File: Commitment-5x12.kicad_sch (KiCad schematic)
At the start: 96 parts, among them J1 Conn_01x13, J2 Conn_01x13, J3 Conn_01x03, J4 Conn_01x04, J5 Conn_01x04, SW1 OS102011MS2QN1, SW2 RotaryEncoder

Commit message: updated footprints to include 3D cad files
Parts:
- J3: footprint lizard_libs:PinHeader_1x03_P2.54mm_Vertical -> lizard_libs:PinSocket_1x03_P2.54mm_Vertical
- MX1, MX10, MX11, MX12, MX13, MX14, MX15, MX16, MX17, MX18, MX19, MX2, MX20, MX21, MX22, MX23, MX24, MX25, MX26, MX27, MX28, MX29, MX3, MX31, MX32, MX33, MX34, MX36, MX37, MX38, MX39, MX4, MX40, MX41, MX42, MX43, MX44, MX45, MX46, MX47, MX48, MX49, MX5, MX50, MX51, MX52, MX53, MX54, MX55, MX56, MX57, MX58, MX59, MX6, MX60, MX7, MX8, MX9: footprint lizard_libs:hotswap_keyswitch_reflow -> lizard_libs:Kailh_MX_Hotswap_Socket

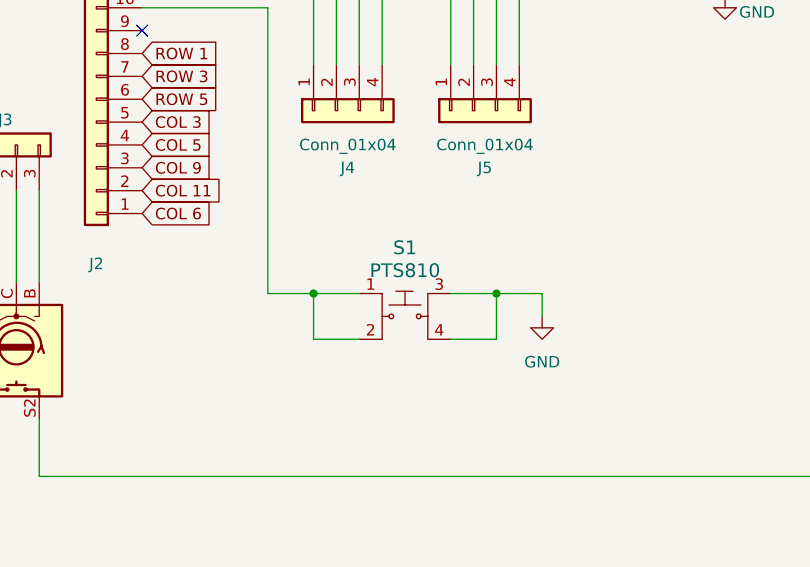
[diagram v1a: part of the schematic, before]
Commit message: Switched to B3F reset switch
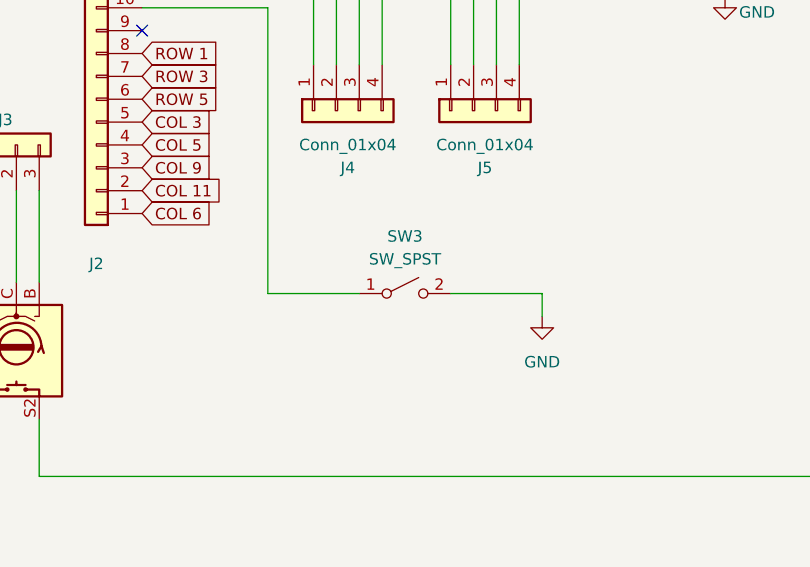
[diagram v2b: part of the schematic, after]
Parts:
- removed S1: PTS810, lizard_libs:PTS_180_Tactile_Switch, symbol lizard_lib:PTS810
- added SW3: SW_SPST, lizard_libs:Omron_B3F-1000, symbol Switch:SW_SPST
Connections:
- net GND: now also SW3.2 (B)
- net at J2.10 (Pin_10): now also SW3.1 (A)
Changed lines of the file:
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@@
 	)
 	(junction
-		(at 130.81 113.03)
-		(diameter 0)
-		(color 0 0 0 0)
-	)
-	(junction
 		(at 163.83 200.66)
 		(diameter 0)
@@
 	)
 	(junction
-		(at 110.49 113.03)
-		(diameter 0)
-		(color 0 0 0 0)
-	)
-	(junction
 		(at 176.53 194.31)
 		(diameter 0)
@@
 	(wire
 		(pts
-			(xy 130.81 118.11) (xy 130.81 113.03)
-		)
-		(stroke
-			(width 0)
-			(type default)
-		)
-	)
-	(wire
-		(pts
 			(xy 213.36 161.29) (xy 213.36 165.1)
 		)
@@
 	(wire
 		(pts
-			(xy 110.49 113.03) (xy 115.57 113.03)
-		)
-		(stroke
-			(width 0)
-			(type default)
-		)
-	)
-	(wire
-		(pts
 			(xy 156.21 80.01) (xy 156.21 78.74)
 		)
@@
 	(wire
 		(pts
-			(xy 110.49 118.11) (xy 115.57 118.11)
-		)
-		(stroke
-			(width 0)
-			(type default)
-		)
-	)
-	(wire
-		(pts
 			(xy 118.11 87.63) (xy 118.11 72.39)
 		)
@@
 	(wire
 		(pts
-			(xy 130.81 113.03) (xy 135.89 113.03)
+			(xy 125.73 113.03) (xy 135.89 113.03)
 		)
 		(stroke
@@
 	(wire
 		(pts
-			(xy 125.73 113.03) (xy 130.81 113.03)
-		)
-		(stroke
-			(width 0)
-			(type default)
-		)
-	)
-	(wire
-		(pts
 			(xy 160.02 212.09) (xy 176.53 212.09)
 		)
@@
 	(wire
 		(pts
-			(xy 105.41 113.03) (xy 110.49 113.03)
+			(xy 105.41 113.03) (xy 115.57 113.03)
 		)
 		(stroke
@@
 	(wire
 		(pts
-			(xy 125.73 118.11) (xy 130.81 118.11)
-		)
-		(stroke
-			(width 0)
-			(type default)
-		)
-	)
-	(wire
-		(pts
 			(xy 66.04 76.2) (xy 44.45 76.2)
 		)
@@
 	(wire
 		(pts
-			(xy 110.49 113.03) (xy 110.49 118.11)
-		)
-		(stroke
-			(width 0)
-			(type default)
-		)
-	)
-	(wire
-		(pts
 			(xy 127 194.31) (xy 143.51 194.31)
 		)
@@
 	)
 	(symbol
+		(lib_id "Switch:SW_SPST")
+		(at 120.65 113.03 0)
+		(unit 1)
+		(exclude_from_sim no)
+		(in_bom yes)
+		(on_board yes)
+		(dnp no)
+		(fields_autoplaced yes)
+		(property "Reference" "SW3"
+			(at 120.65 106.68 0)
+			(effects
+				(font
+					(size 1.27 1.27)
+				)
+			)
+		)
+		(property "Value" "SW_SPST"
+			(at 120.65 109.22 0)
+			(effects
+				(font
+					(size 1.27 1.27)
+				)
+			)
+		)
+		(property "Footprint" "lizard_libs:Omron_B3F-1000"
+			(at 120.65 113.03 0)
+			(effects
+				(font
+					(size 1.27 1.27)
+				)
+				(hide yes)
+			)
+		)
+		(property "Datasheet" "~"
+			(at 120.65 113.03 0)
+			(effects
+				(font
+					(size 1.27 1.27)
+				)
+				(hide yes)
+			)
+		)
+		(property "Description" "Single Pole Single Throw (SPST) switch"
+			(at 120.65 113.03 0)
+			(effects
+				(font
+					(size 1.27 1.27)
+				)
+				(hide yes)
+			)
+		)
+		(pin "1"
+		)
+		(pin "2"
+		)
+		(instances
+			(project ""
+				(path "/0dc486c7-2743-451e-93ad-8516174ce902"
+					(reference "SW3")
+					(unit 1)
+				)
+			)
+		)
+	)
+	(symbol
 		(lib_id "lizard_lib:MX_Switch")
 		(at 104.14 166.37 0)
@@
 					(unit 1)
 				)
-			)
-		)
-	)
-	(symbol
-		(lib_id "lizard_lib:PTS810")
-		(at 120.65 115.57 0)
-		(unit 1)
-		(exclude_from_sim no)
-		(in_bom yes)
-		(on_board yes)
-		(dnp no)
-		(fields_autoplaced yes)
-		(property "Reference" "S1"
-			(at 120.65 107.95 0)
-			(effects
-				(font
-					(size 1.524 1.524)
-				)
-			)
-		)
-		(property "Value" "PTS810"
-			(at 120.65 110.49 0)
-			(effects
-				(font
-					(size 1.524 1.524)
-				)
-			)
-		)
-		(property "Footprint" "lizard_libs:PTS_180_Tactile_Switch"
-			(at 125.73 110.49 0)
-			(effects
-				(font
-					(size 1.524 1.524)
-				)
-				(justify left)
-				(hide yes)
-			)
-		)
-		(property "Datasheet" ""
-			(at 125.73 107.95 0)
-			(effects
-				(font
-					(size 1.524 1.524)
-				)
-				(justify left)
-				(hide yes)
-			)
-		)
-		(property "Description" "SWITCH TACTILE SPST-NO 0.05A 24V"
-			(at 120.65 115.57 0)
-			(effects
-				(font
-					(size 1.27 1.27)
-				)
-				(hide yes)
-			)
-		)
-		(property "Location" "Denali-H2"
-			(at 120.65 115.57 0)
-			(effects
-				(font
-					(size 1.27 1.27)
-				)
-				(hide yes)
-			)
-		)
-		(pin "4"
-		)
-		(pin "1"
-		)
-		(pin "2"
-		)
-		(pin "3"
-		)
-		(instances
-			(project ""
-				(path "/0dc486c7-2743-451e-93ad-8516174ce902"
-					(reference "S1")
-					(unit 1)
-				)

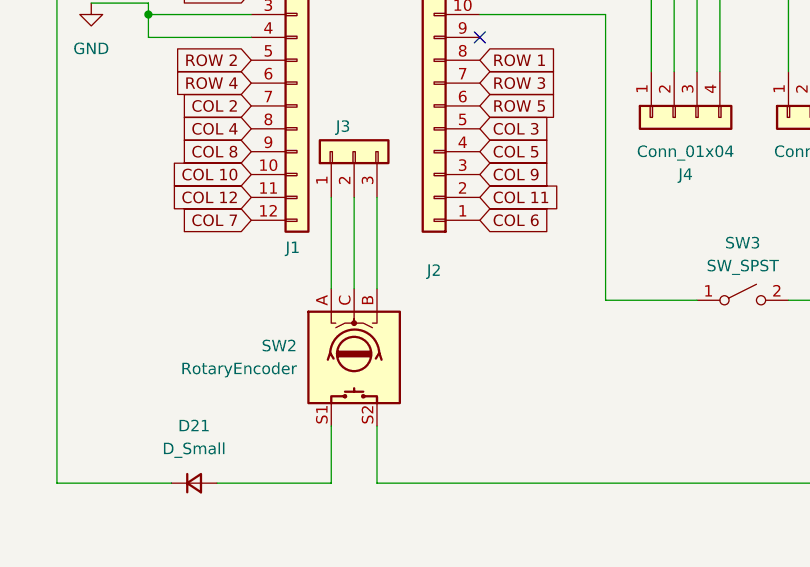
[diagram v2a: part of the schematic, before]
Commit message: Disconnected encoder C from microcontroller and connected it to ground
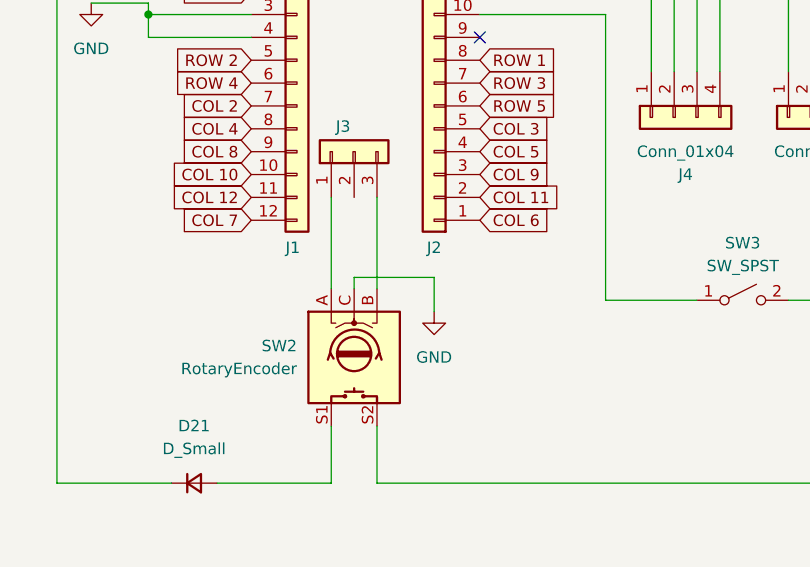
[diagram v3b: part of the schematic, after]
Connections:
- net GND: now also SW2.C
- net at J3.2 (Pin_2): no longer SW2.C
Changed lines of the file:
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@@
 	(wire
 		(pts
+			(xy 77.47 111.76) (xy 77.47 110.49)
+		)
+		(stroke
+			(width 0)
+			(type default)
+		)
+	)
+	(wire
+		(pts
 			(xy 208.28 161.29) (xy 213.36 161.29)
 		)
@@
 	(wire
 		(pts
+			(xy 77.47 110.49) (xy 86.36 110.49)
+		)
+		(stroke
+			(width 0)
+			(type default)
+		)
+	)
+	(wire
+		(pts
 			(xy 130.81 182.88) (xy 130.81 200.66)
 		)
@@
 	(wire
 		(pts
+			(xy 86.36 110.49) (xy 86.36 114.3)
+		)
+		(stroke
+			(width 0)
+			(type default)
+		)
+	)
+	(wire
+		(pts
 			(xy 110.49 212.09) (xy 127 212.09)
 		)
@@
 	(wire
 		(pts
-			(xy 77.47 101.6) (xy 77.47 111.76)
-		)
-		(stroke
-			(width 0)
-			(type default)
-		)
-	)
-	(wire
-		(pts
 			(xy 213.36 200.66) (xy 213.36 218.44)
 		)
@@
 		(dnp no)
 		(property "Reference" "J2"
-			(at 86.36 109.728 0)
+			(at 86.36 107.188 0)
 			(effects
 				(font
@@
 					(unit 1)
 				)
+			)
+		)
+	)
+	(symbol
+		(lib_id "power:GND")
+		(at 86.36 114.3 0)
+		(unit 1)
+		(exclude_from_sim no)
+		(in_bom yes)
+		(on_board yes)
+		(dnp no)
+		(fields_autoplaced yes)
+		(property "Reference" "#PWR04"
+			(at 86.36 120.65 0)
+			(effects
+				(font
+					(size 1.27 1.27)
+				)
+				(hide yes)
+			)
+		)
+		(property "Value" "GND"
+			(at 86.36 119.38 0)
+			(effects
+				(font
+					(size 1.27 1.27)
+				)
+			)
+		)
+		(property "Footprint" ""
+			(at 86.36 114.3 0)
+			(effects
+				(font
+					(size 1.27 1.27)
+				)
+				(hide yes)
+			)
+		)
+		(property "Datasheet" ""
+			(at 86.36 114.3 0)
+			(effects
+				(font
+					(size 1.27 1.27)
+				)
+				(hide yes)
+			)
+		)
+		(property "Description" "Power symbol creates a global label with name \"GND\" , ground"
+			(at 86.36 114.3 0)
+			(effects
+				(font
+					(size 1.27 1.27)
+				)
+				(hide yes)
+			)
+		)
+		(pin "1"
+		)
+		(instances
+			(project "Commitment-5x12"
+				(path "/0dc486c7-2743-451e-93ad-8516174ce902"
+					(reference "#PWR04")
+					(unit 1)
+				)
